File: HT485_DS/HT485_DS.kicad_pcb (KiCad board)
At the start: 2 copper layers, 24.2 x 24.2 mm, 4 parts, among them J1 H/T Sensor, U1 SHT31A-DIS

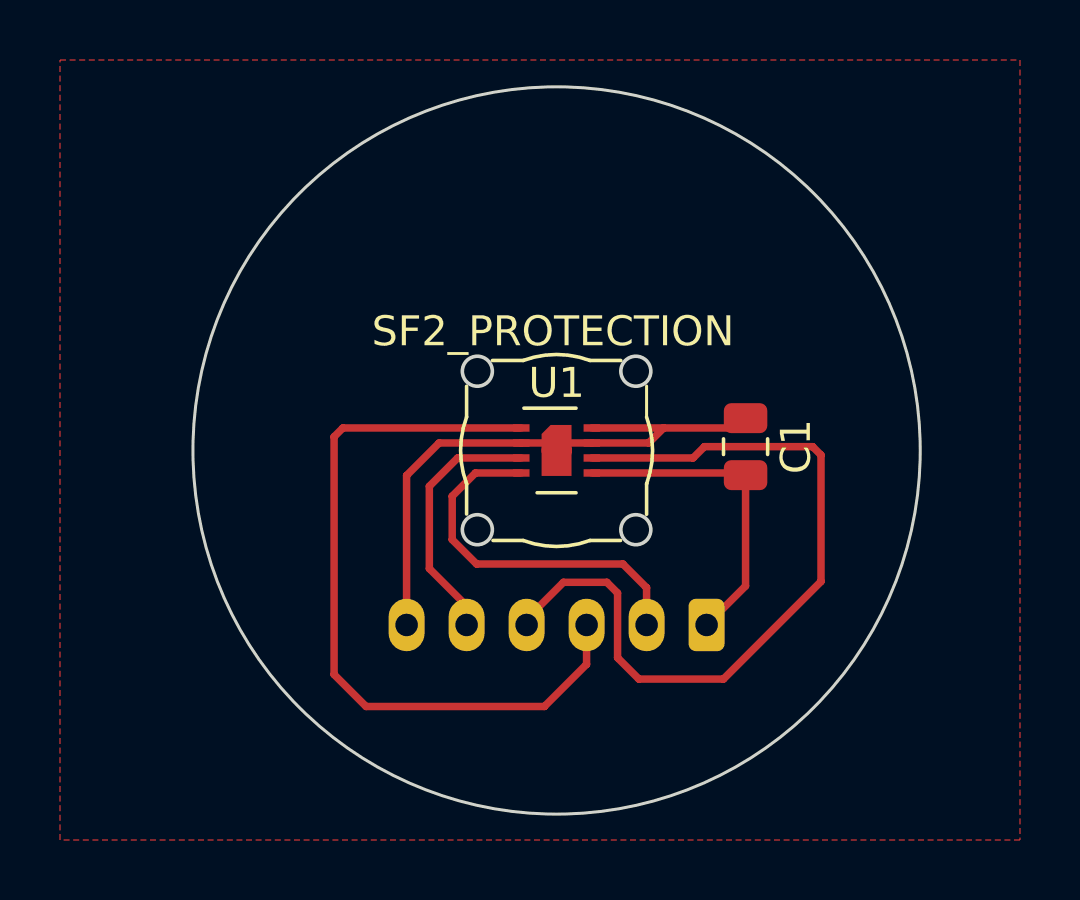
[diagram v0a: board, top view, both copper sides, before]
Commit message: Aggiornato gerber
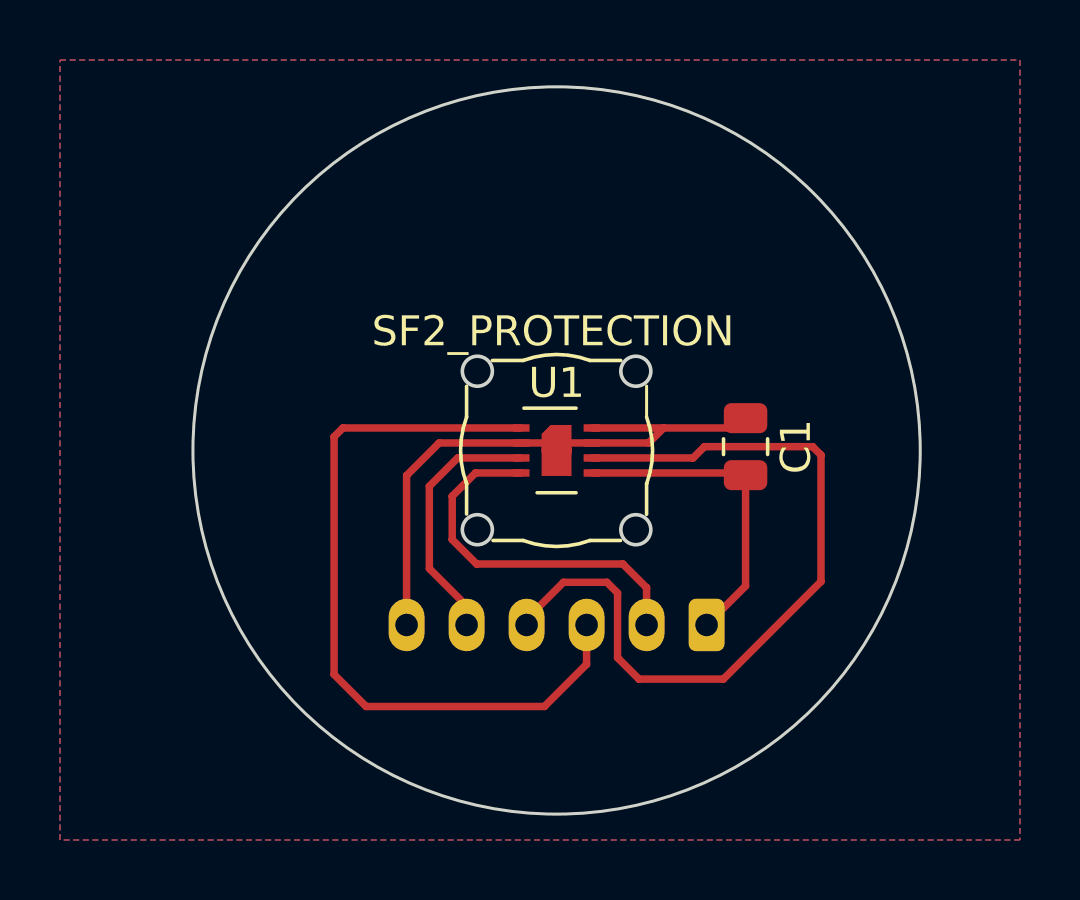
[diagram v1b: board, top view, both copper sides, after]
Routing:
- added copper zone on B.Cu, net GND
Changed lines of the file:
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@@
   (segment (start 102.3112 75.2094) (end 103.255 74.2656) (width 0.25) (layer "F.Cu") (net 6))
   (segment (start 102.3112 77.9526) (end 102.3112 75.2094) (width 0.25) (layer "F.Cu") (net 6))
-  (zone (net 1) (net_name "GND") (layer "F.Cu") (hatch edge 0.508)
+  (zone (net 1) (net_name "GND") (layers F&B.Cu) (hatch edge 0.508)
     (connect_pads yes (clearance 0.508))
     (min_thickness 0.254) (filled_areas_thickness no)

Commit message: Rimosso piano di massa da sensore T/H digitale Aggiunti dati per produzione JLCPCB
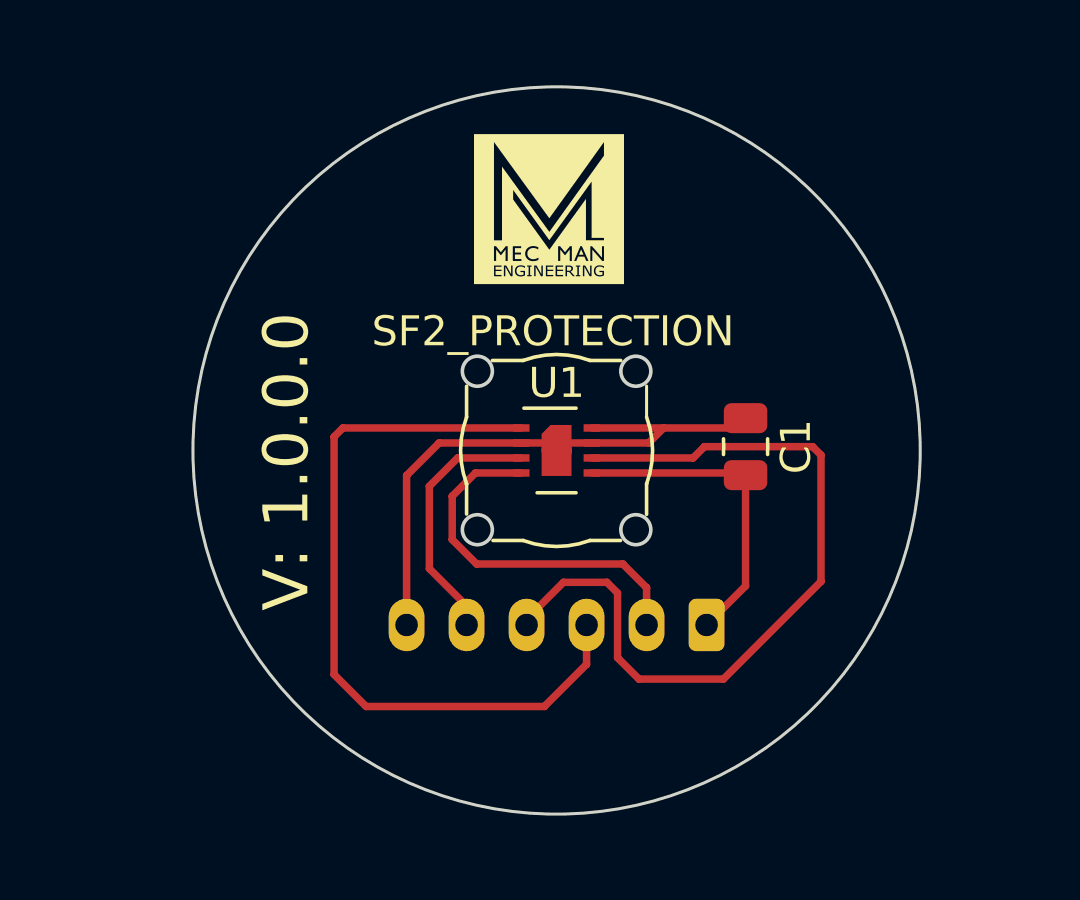
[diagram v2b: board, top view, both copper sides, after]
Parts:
- added REF**: MME_LOGO_5x5, HT485:MME_LOGO_5x5, F.Cu at (106.3, 66.0)
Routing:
- removed copper zone on B.Cu, net GND
- removed copper zone on F.Cu, net GND
